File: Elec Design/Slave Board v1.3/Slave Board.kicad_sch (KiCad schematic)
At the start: 83 parts, among them J3 1935174, J6 61300411121, J7 Conn_ARM_JTAG_SWD_10, J8 1935161, J9 1935161, M1 VID28-05, M2 VID28-05, M3 VID28-05, M4 VID28-05, SW1 SW_SPST, U1 LPC11C24-LQFP48, U10 DRV5033AJxDBZ, U11 DRV5033AJxDBZ, U14 BD9E302EFJ-E2, U15 NCP718xSN330, U2 VID6606, U3 VID6606, U4 DRV5033AJxDBZ, U5 DRV5033AJxDBZ, U6 DRV5033AJxDBZ, U7 DRV5033AJxDBZ, U8 DRV5033AJxDBZ, U9 DRV5033AJxDBZ, Y1 12MHz/12pF

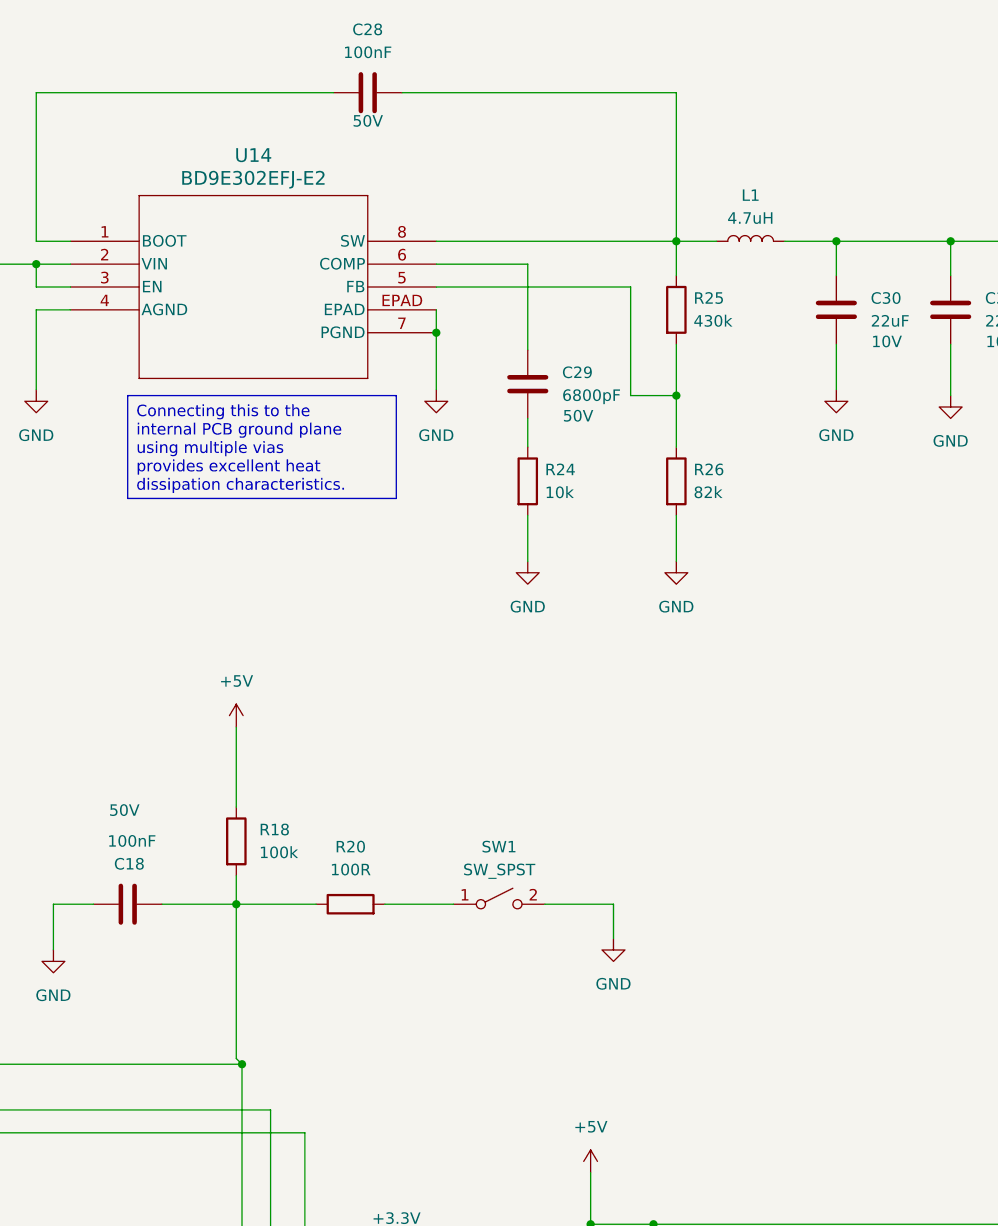
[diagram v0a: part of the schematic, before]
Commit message: fixed buck converter feedback position error
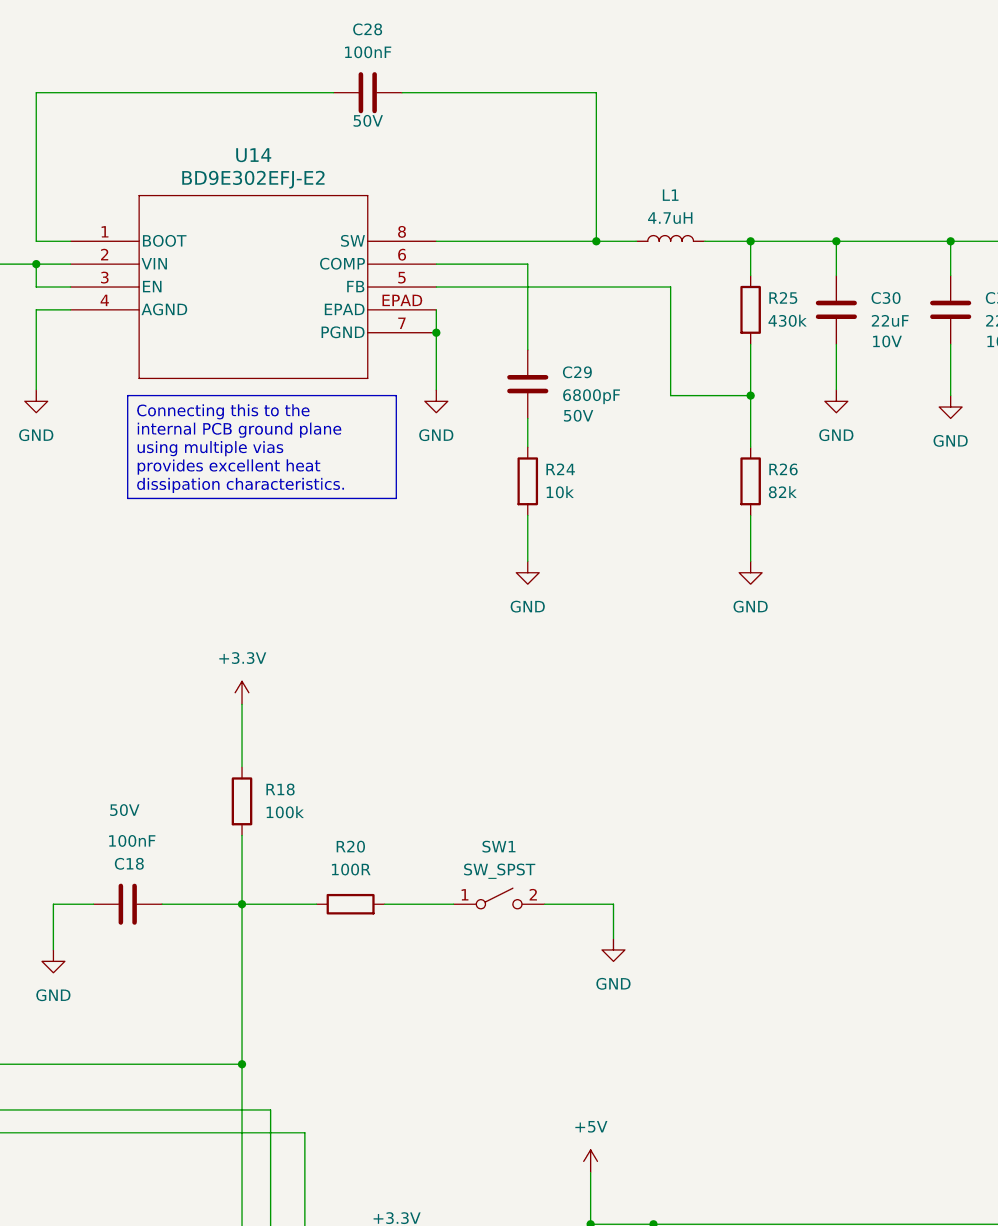
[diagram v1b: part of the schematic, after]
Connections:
- net +3.3V: now also R18.1
- net +5V: now also R25.1; no longer R18.1
- net at C28.2, L1.1, U14.8 (SW): no longer R25.1
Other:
- moved on the sheet: L1, R18, R25, R26

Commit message: Changed FB position on 5v output - after caps
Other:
- note added: "Do these need to be pulldown?"
- moved on the sheet: C30, C31, R25, R26

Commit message: schematic changes to include level shifter
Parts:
- added U12, U13: SN74LVC245APW, Package_SO:TSSOP-20_4.4x6.5mm_P0.65mm, symbol Logic_LevelTranslator:SN74LVC245APW
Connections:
- net +3.3V: no longer U5.1 (VCC)
- net +5V: now also U12.20 (VCC), U13.20 (VCC)
- net CW/~{CCWA} - 1: now also U12.2 (A1); no longer U2.27 (CW/~{CCWA})
- net CW/~{CCWA} - 2: now also U13.2 (A1); no longer U3.27 (CW/~{CCWA})
- net CW/~{CCWB} - 1: now also U12.4 (A3); no longer U2.2 (CW/~{CCWB})
- net CW/~{CCWB} - 2: now also U13.4 (A3); no longer U3.2 (CW/~{CCWB})
- net CW/~{CCWC} - 1 : now also U12.6 (A5); no longer U2.13 (CW/~{CCWC})
- net CW/~{CCWC} - 2: now also U13.6 (A5); no longer U3.13 (CW/~{CCWC})
- net CW/~{CCWD} - 1: now also U12.8 (A7); no longer U2.16 (CW/~{CCWD})
- net CW/~{CCWD} - 2: now also U13.8 (A7); no longer U3.16 (CW/~{CCWD})
- net F(SCX)A - 1 : now also U12.3 (A2); no longer U2.28 (F(SCX)A)
- net F(SCX)A - 2: now also U13.3 (A2); no longer U3.28 (F(SCX)A)
- net F(SCX)B - 1 : now also U12.5 (A4); no longer U2.3 (F(SCX)B)
- net F(SCX)B - 2: now also U13.5 (A4); no longer U3.3 (F(SCX)B)
- net F(SCX)C - 1 : now also U12.7 (A6); no longer U2.14 (F(SCX)C)
- net F(SCX)C - 2: now also U13.7 (A6); no longer U3.14 (F(SCX)C)
- net F(SCX)D - 1 : now also U12.9 (A8); no longer U2.17 (F(SCX)D)
- net F(SCX)D - 2: now also U13.9 (A8); no longer U3.17 (F(SCX)D)
- net GND: now also U12.10 (GND), U13.10 (GND); no longer U5.3 (GND)
- net HAll A Min - 1 : no longer U5.2 (OUT)
- new net: U12.14 (B5), U2.13 (CW/~{CCWC})
- new net: U12.13 (B6), U2.14 (F(SCX)C)
- new net: U12.12 (B7), U2.16 (CW/~{CCWD})
- new net: U12.11 (B8), U2.17 (F(SCX)D)
- new net: U12.16 (B3), U2.2 (CW/~{CCWB})
- new net: U12.18 (B1), U2.27 (CW/~{CCWA})
- new net: U12.17 (B2), U2.28 (F(SCX)A)
- new net: U12.15 (B4), U2.3 (F(SCX)B)
- new net: U13.14 (B5), U3.13 (CW/~{CCWC})
- new net: U13.13 (B6), U3.14 (F(SCX)C)
- new net: U13.12 (B7), U3.16 (CW/~{CCWD})
- new net: U13.11 (B8), U3.17 (F(SCX)D)
- new net: U13.16 (B3), U3.2 (CW/~{CCWB})
- new net: U13.18 (B1), U3.27 (CW/~{CCWA})
- new net: U13.17 (B2), U3.28 (F(SCX)A)
- new net: U13.15 (B4), U3.3 (F(SCX)B)
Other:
- note removed: "Do these need to be pulldown?"
- moved on the sheet: C1, C10, C11, C12, C13, C16, C18, C19, C2, C21, C22, C23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

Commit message: pre ketan updates
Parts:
- added C14, C15, C17, C20: 0.1uF, Capacitor_SMD:C_0603_1608Metric, symbol Device:C
- added R35, R36: 10k, Resistor_SMD:R_0603_1608Metric, symbol Device:R
- R10, R11, R12, R13, R6, R7, R8, R9: now not fitted; now left out of the parts list
- U12, U13: value SN74LVC245APW -> SN74LVC8T245; footprint Package_SO:TSSOP-20_4.4x6.5mm_P0.65mm -> Package_SO:TSSOP-24_4.4x7.8mm_P0.65mm; symbol Logic_LevelTranslator:SN74LVC245APW -> Logic_LevelTranslator:SN74LVC8T245
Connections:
- net +3.3V: now also U12.1 (V_{CCA}), U13.1 (V_{CCA}), U5.1 (VCC), C14.2, C17.2, R35.1, R36.1
- net +5V: now also U12.23 (V_{CCB}), U12.24 (V_{CCB}), U13.23 (V_{CCB}), U13.24 (V_{CCB}), C15.2, C20.2; no longer U12.20 (VCC), U13.20 (VCC)
- net CW/~{CCWA} - 1: now also U12.3 (A1); no longer U12.2 (A1)
- net CW/~{CCWA} - 2: now also U13.3 (A1); no longer U13.2 (A1)
- net CW/~{CCWB} - 1: now also U12.5 (A3); no longer U12.4 (A3)
- net CW/~{CCWB} - 2: now also U13.5 (A3); no longer U13.4 (A3)
- net CW/~{CCWC} - 1 : now also U12.7 (A5); no longer U12.6 (A5)
- net CW/~{CCWC} - 2: now also U13.7 (A5); no longer U13.6 (A5)
- net CW/~{CCWD} - 1: now also U12.9 (A7); no longer U12.8 (A7)
- net CW/~{CCWD} - 2: now also U13.9 (A7); no longer U13.8 (A7)
- net F(SCX)A - 1 : now also U12.4 (A2); no longer U12.3 (A2)
- net F(SCX)A - 2: now also U13.4 (A2); no longer U13.3 (A2)
- net F(SCX)B - 1 : now also U12.6 (A4); no longer U12.5 (A4)
- net F(SCX)B - 2: now also U13.6 (A4); no longer U13.5 (A4)
- net F(SCX)C - 1 : now also U12.8 (A6); no longer U12.7 (A6)
- net F(SCX)C - 2: now also U13.8 (A6); no longer U13.7 (A6)
- net F(SCX)D - 1 : now also U12.10 (A8); no longer U12.9 (A8)
- net F(SCX)D - 2: now also U13.10 (A8); no longer U13.9 (A8)
- net GND: now also U12.11 (GND), U12.12 (GND), U12.13 (GND), U12.22 (~{OE}), U13.11 (GND), U13.12 (GND), U13.13 (GND), U13.22 (~{OE}), U5.3 (GND), C14.1, C15.1, C17.1, C20.1; no longer U12.10 (GND), U13.10 (GND)
- net HAll A Min - 1 : now also U5.2 (OUT)
- net at U2.13 (CW/~{CCWC}): now also U12.17 (B5); no longer U12.14 (B5)
- net at U2.14 (F(SCX)C): now also U12.16 (B6); no longer U12.13 (B6)
- net at U2.16 (CW/~{CCWD}): now also U12.15 (B7); no longer U12.12 (B7)
- net at U2.17 (F(SCX)D): now also U12.14 (B8); no longer U12.11 (B8)
- net at U2.2 (CW/~{CCWB}): now also U12.19 (B3); no longer U12.16 (B3)
- net at U2.27 (CW/~{CCWA}): now also U12.21 (B1); no longer U12.18 (B1)
- net at U2.28 (F(SCX)A): now also U12.20 (B2); no longer U12.17 (B2)
- net at U2.3 (F(SCX)B): now also U12.18 (B4); no longer U12.15 (B4)
- net at U3.13 (CW/~{CCWC}): now also U13.17 (B5); no longer U13.14 (B5)
- net at U3.14 (F(SCX)C): now also U13.16 (B6); no longer U13.13 (B6)
- net at U3.16 (CW/~{CCWD}): now also U13.15 (B7); no longer U13.12 (B7)
- net at U3.17 (F(SCX)D): now also U13.14 (B8); no longer U13.11 (B8)
- net at U3.2 (CW/~{CCWB}): now also U13.19 (B3); no longer U13.16 (B3)
- net at U3.27 (CW/~{CCWA}): now also U13.21 (B1); no longer U13.18 (B1)
- net at U3.28 (F(SCX)A): now also U13.20 (B2); no longer U13.17 (B2)
- net at U3.3 (F(SCX)B): now also U13.18 (B4); no longer U13.15 (B4)
- new net: R36.2, U13.2 (DIR)
- new net: R35.2, U12.2 (DIR)
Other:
- moved on the sheet: C18, R18, R20, SW1, U5
